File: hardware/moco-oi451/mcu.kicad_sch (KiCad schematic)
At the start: 14 parts, among them SW1 RESET, U2 STM32G431CBUx, Y1 8MHz

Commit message: Reroute and reduce size to Ø40mm
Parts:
- SW1: footprint Button_Switch_SMD:SW_SPST_TL3342 -> Button_Switch_SMD:SW_SPST_CK_RS282G05A3
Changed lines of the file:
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@@
       (effects (font (size 1.27 1.27)) (justify right))
     )
-    (property "Footprint" "Button_Switch_SMD:SW_SPST_TL3342" (at 54.61 76.2 0)
+    (property "Footprint" "Button_Switch_SMD:SW_SPST_CK_RS282G05A3" (at 54.61 76.2 0)
       (effects (font (size 1.27 1.27)) hide)
     )

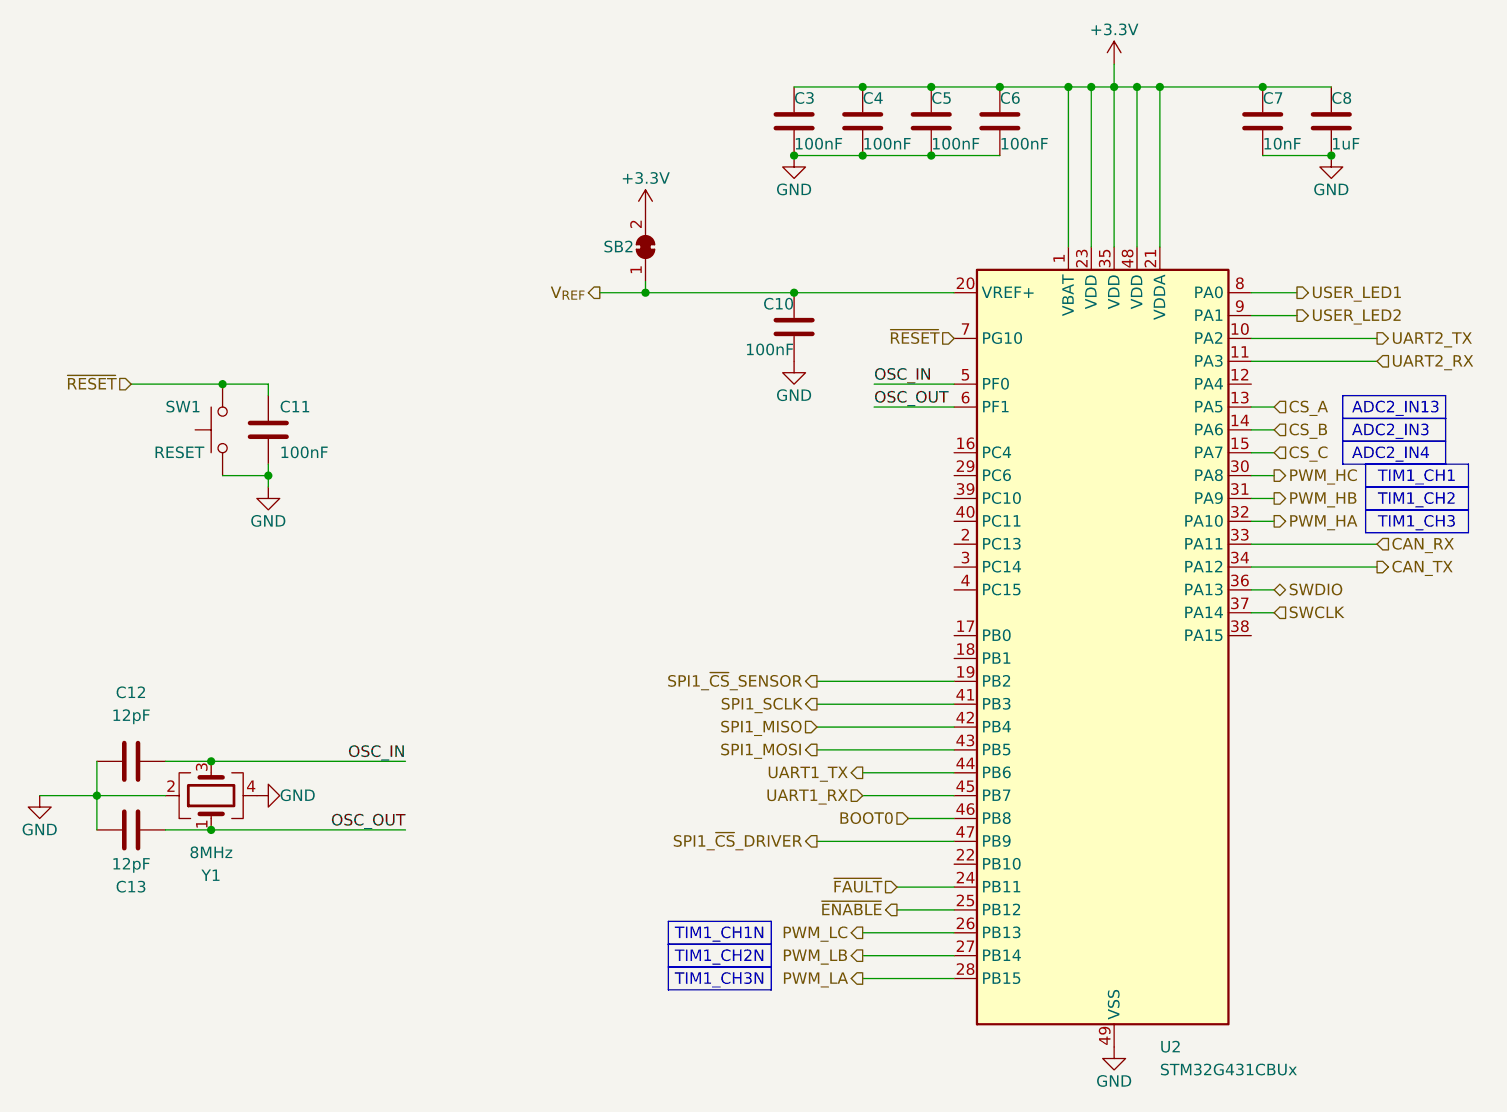
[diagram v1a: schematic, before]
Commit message: Optimize routing
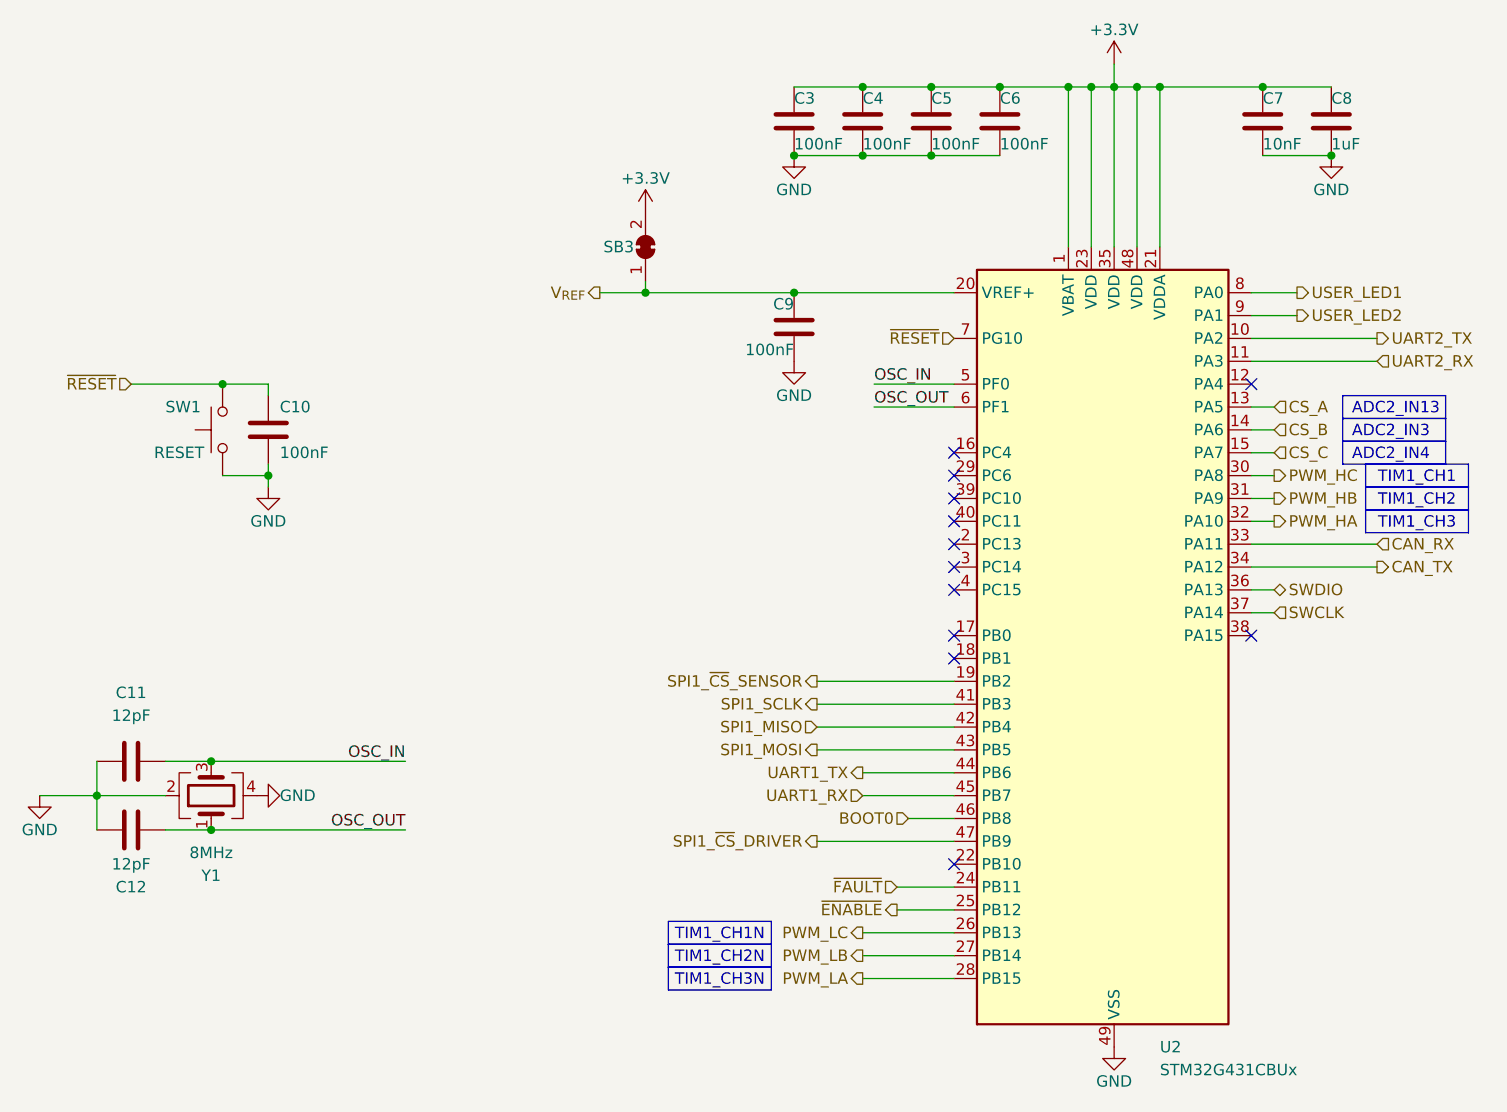
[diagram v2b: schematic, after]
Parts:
- renumbered C11 to C10, C12 to C11, C13 to C12, C10 to C9, SB2 to SB3
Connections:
- no-connect marks 0 -> 12
